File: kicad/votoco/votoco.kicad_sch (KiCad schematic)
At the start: 98 parts, among them J1 Conn_01x02, J10 Conn_01x02, J11 Conn_01x02, J12 Conn_01x02, J13 Conn_01x02, J14 Conn_01x02, J2 Conn_01x04, J3 Conn_02x05_Odd_Even, J4 Conn_01x03, J5 Conn_01x02, J6 Conn_01x02, J7 Conn_01x02, J8 Conn_01x03, J9 USB_B_Micro, Q1 RQ6E045TN, Q2 RQ6E045TN, Q3 RQ6E045TN, SW1 Reset, SW2 Boot, U1 SN65HVD231, U2 TMC2209-LA-T, U3 STM32F042G6Ux, U4 74AHC1G08, U5 MAX2040xAFL, U6 NCP1117-3.3, U7 ADXL345BCCZ, Y1 12Mhz

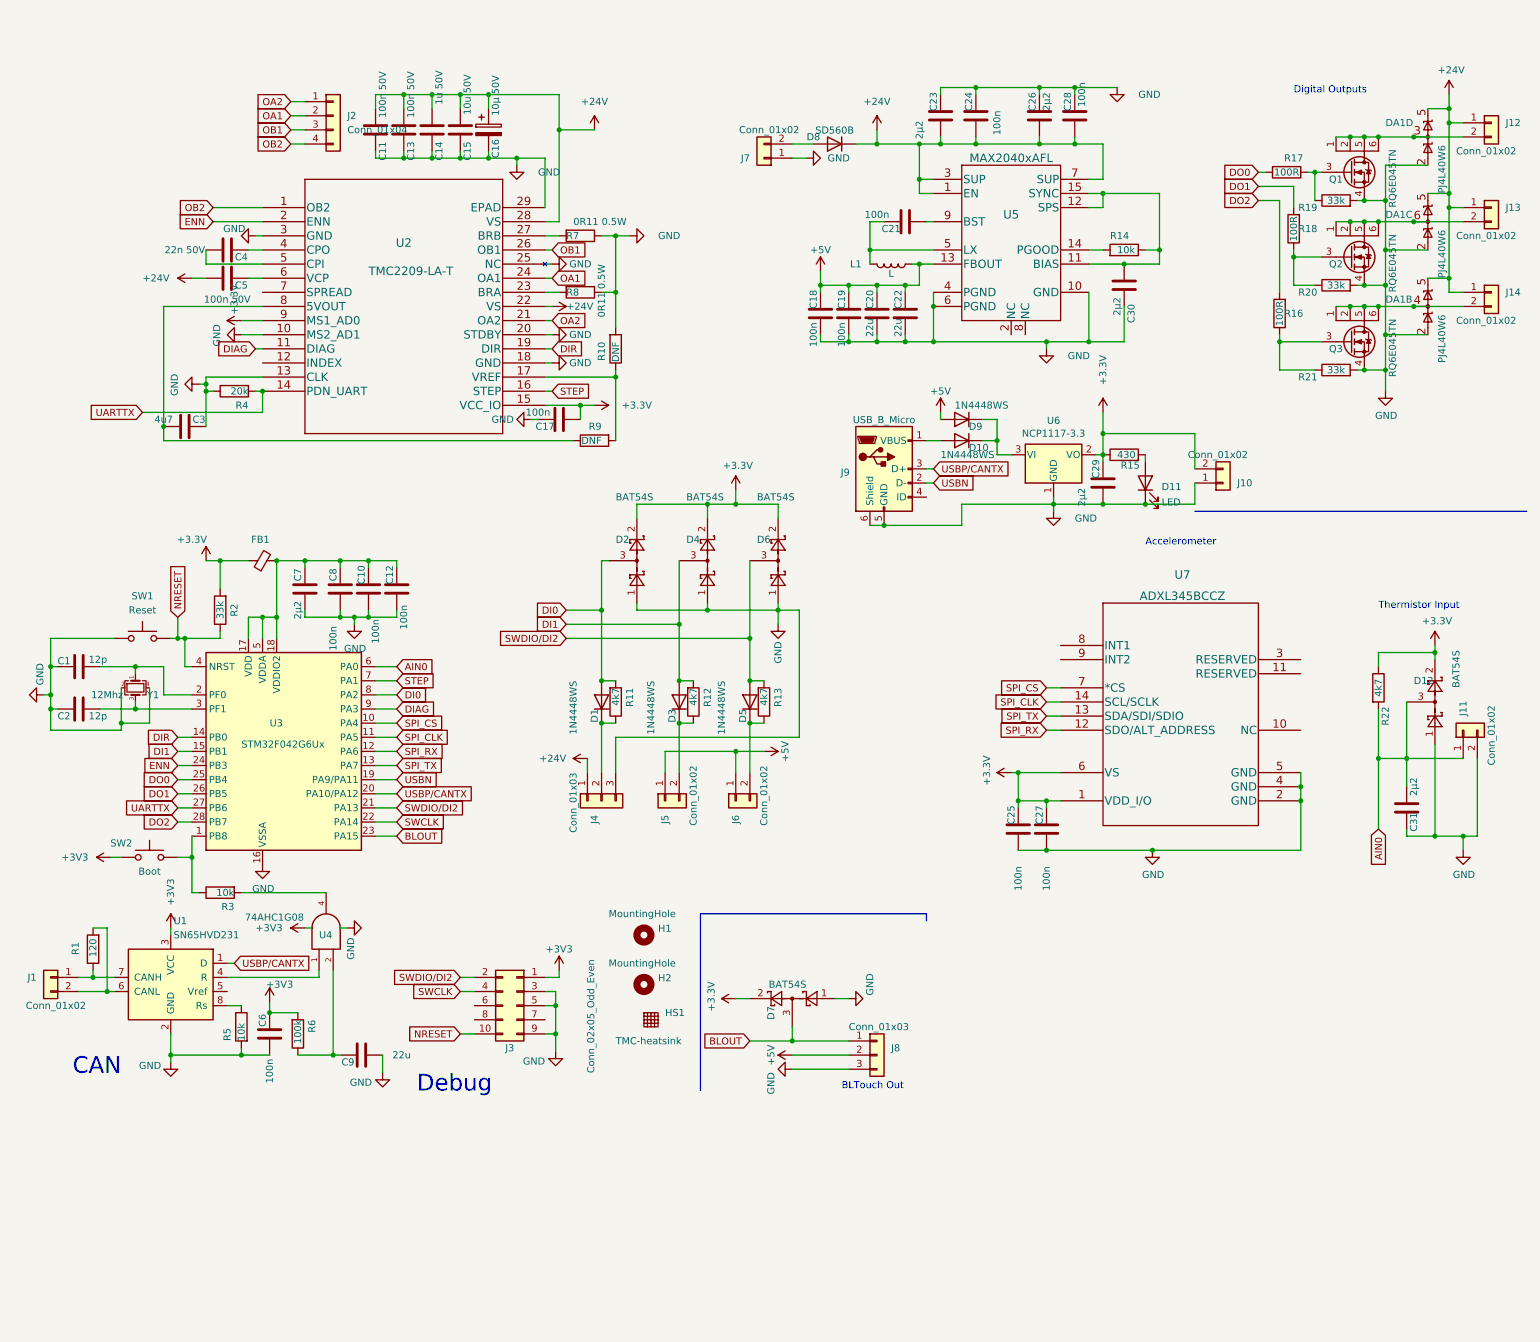
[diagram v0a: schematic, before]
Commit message: some error from V1.0 corrected
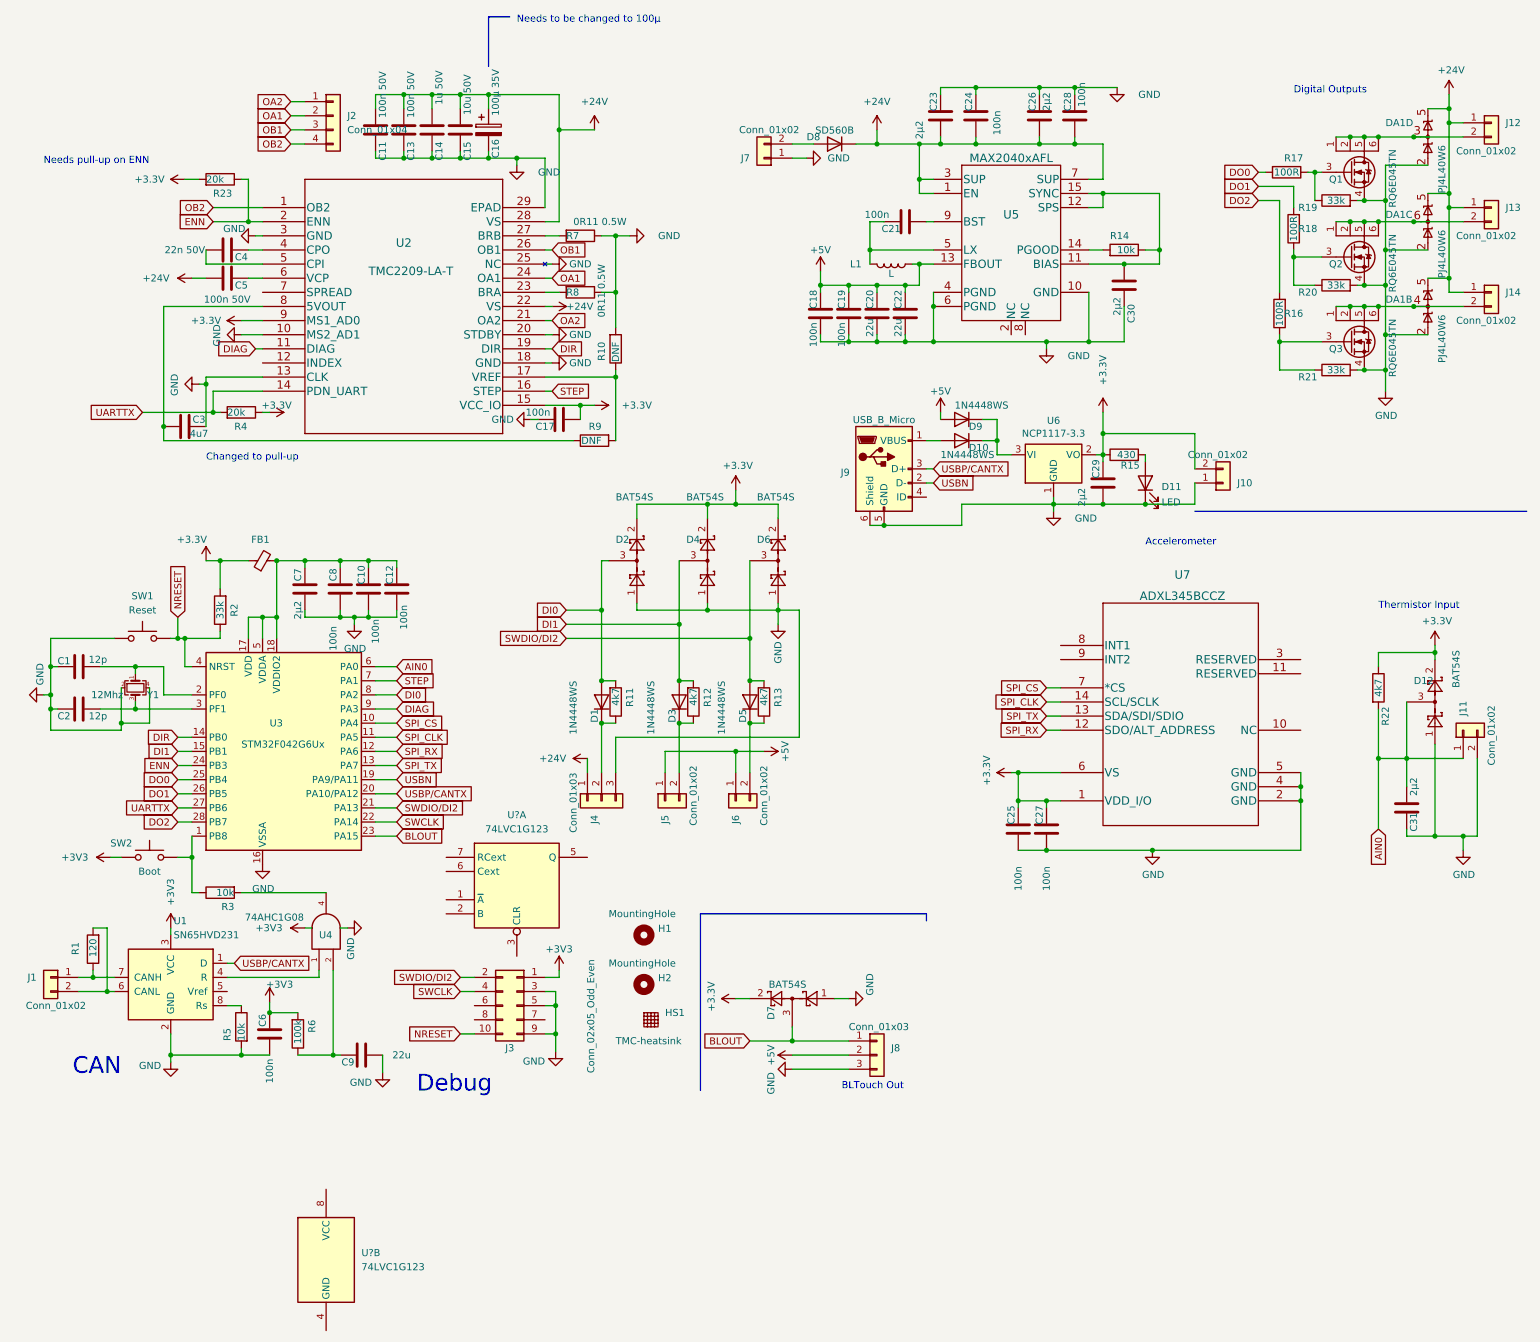
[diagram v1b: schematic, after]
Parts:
- added R23: 20k, Resistor_SMD:R_0603_1608Metric, symbol Device:R
- added U? (x2): 74LVC1G123, symbol 74xGxx:74LVC1G123
- C16: value 10µ 50V -> 100µ 35V; footprint Capacitor_SMD:CP_Elec_4x3 -> Capacitor_SMD:CP_Elec_6.3x7.7
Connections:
- net +3V3: now also R4.1, R23.2
- net ENN: now also R23.1
- net GND: no longer R4.1
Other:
- note added: "Changed to pull-up"
- note added: "Needs pull-up on ENN"
- note added: "Needs to be changed to 100µ"
- moved on the sheet: R4

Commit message: switched to new mcu
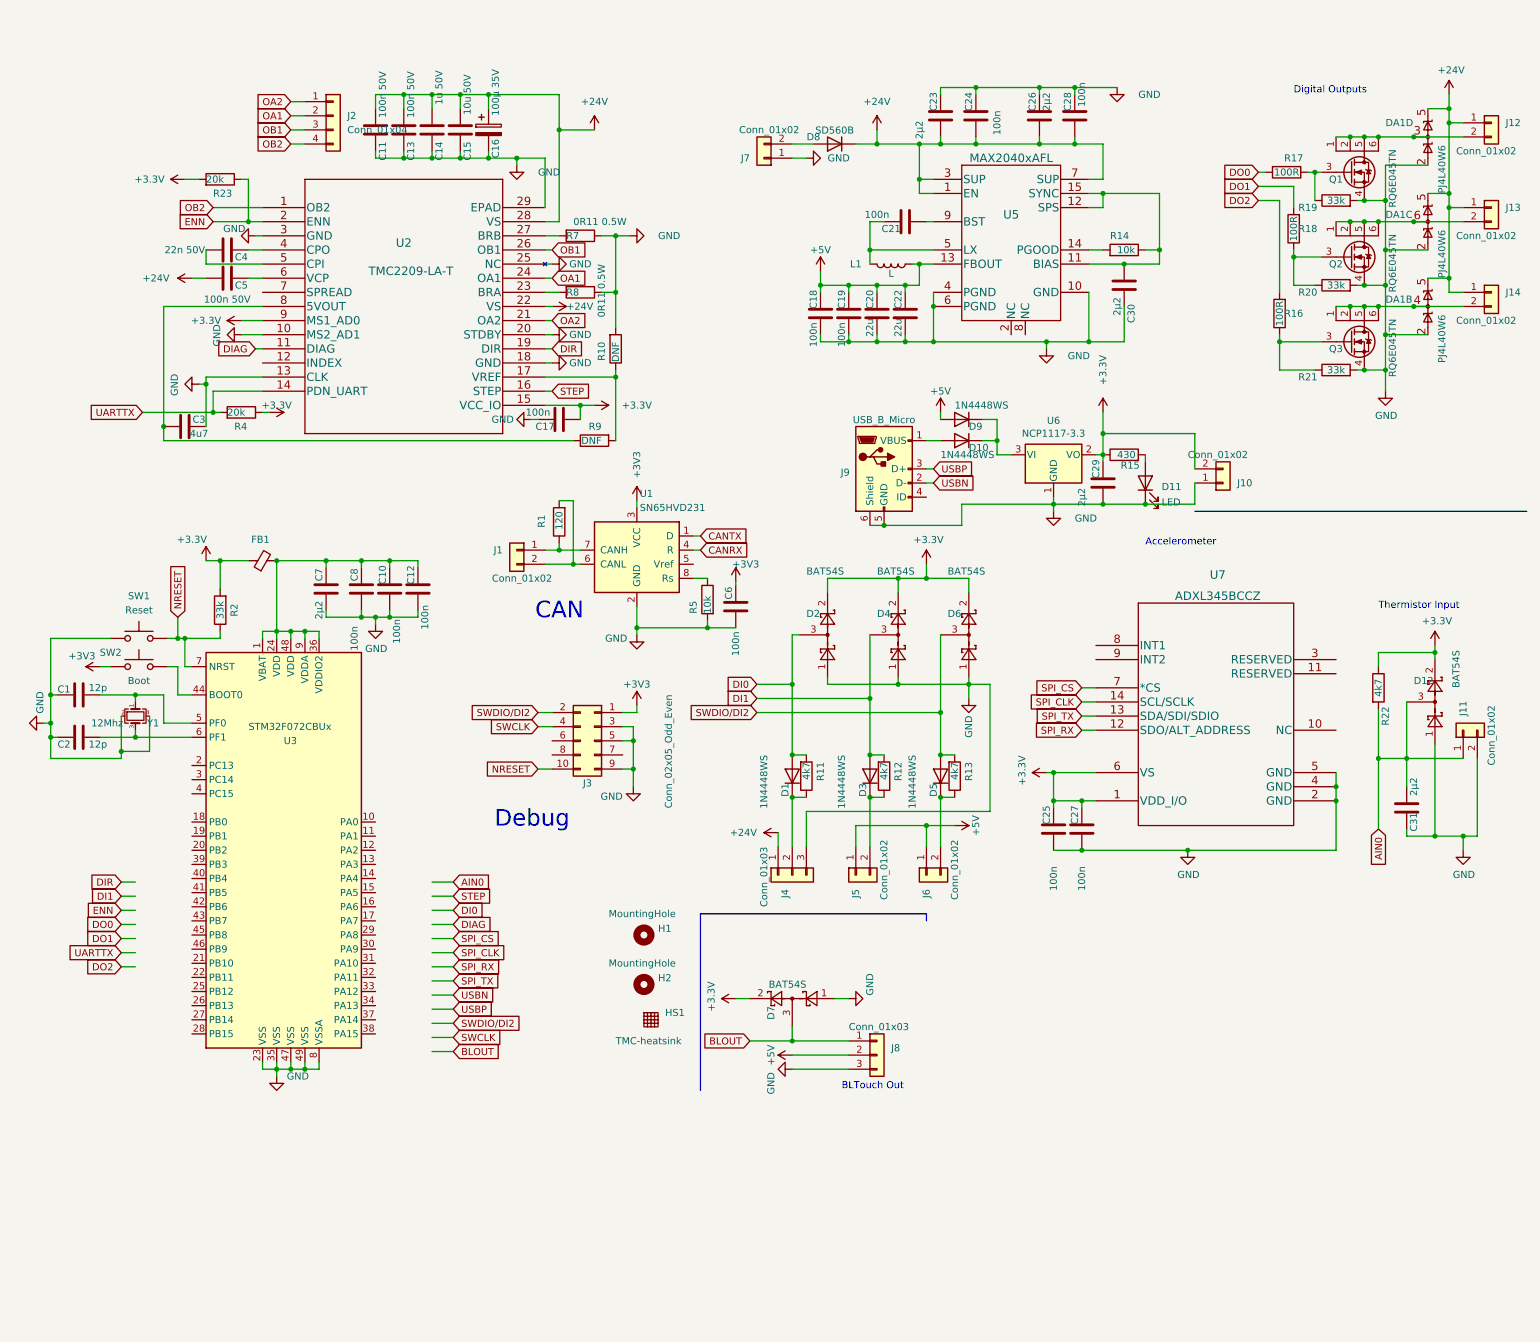
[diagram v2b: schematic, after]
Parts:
- removed C9: 22u, Capacitor_SMD:C_0603_1608Metric, symbol Device:C
- removed R3: 10k, Resistor_SMD:R_0603_1608Metric, symbol Device:R
- removed R6: 100k, Resistor_SMD:R_0603_1608Metric, symbol Device:R
- removed U3: STM32F042G6Ux, Package_DFN_QFN:QFN-28_4x4mm_P0.5mm, symbol MCU_ST_STM32F0:STM32F042G6Ux
- removed U4: 74AHC1G08, Package_TO_SOT_SMD:SOT-353_SC-70-5, symbol 74xGxx:74AHC1G08
- removed U? (x2): 74LVC1G123, symbol 74xGxx:74LVC1G123
- added U3: STM32F072CBUx, Package_DFN_QFN:QFN-48-1EP_7x7mm_P0.5mm_EP5.6x5.6mm, symbol MCU_ST_STM32F0:STM32F072CBUx
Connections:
- net GND: now also U3.23 (VSS), U3.35 (VSS), U3.47 (VSS), U3.49 (VSS), U3.8 (VSSA)
- net NRESET: now also U3.7 (NRST)
- net at C10.1, C12.1, C7.1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: now also U3.1 (VBAT), U3.24 (VDD), U3.36 (VDDIO2), U3.48 (VDD), U3.9 (VDDA)
- net at SW2.2: now also U3.44 (BOOT0)
- net at C1.2, Y1.1: now also U3.5 (PF0)
- net at C2.2, Y1.3: now also U3.6 (PF1)
- net CANRX: now reaches U1.4 (R)
- net USBP/CANTX renamed CANTX
- net CANTX: no longer J9.3 (D+)
- new net USBP: J9.3 (D+)
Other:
- note removed: "Changed to pull-up"
- note removed: "Needs pull-up on ENN"
- note removed: "Needs to be changed to 100µ"
- moved on the sheet: C1, C10, C12, C2, C25, C27, C6, C7, C8, D1, D2, D3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

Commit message: temp sensor added / I2C connector added / layout almost finished
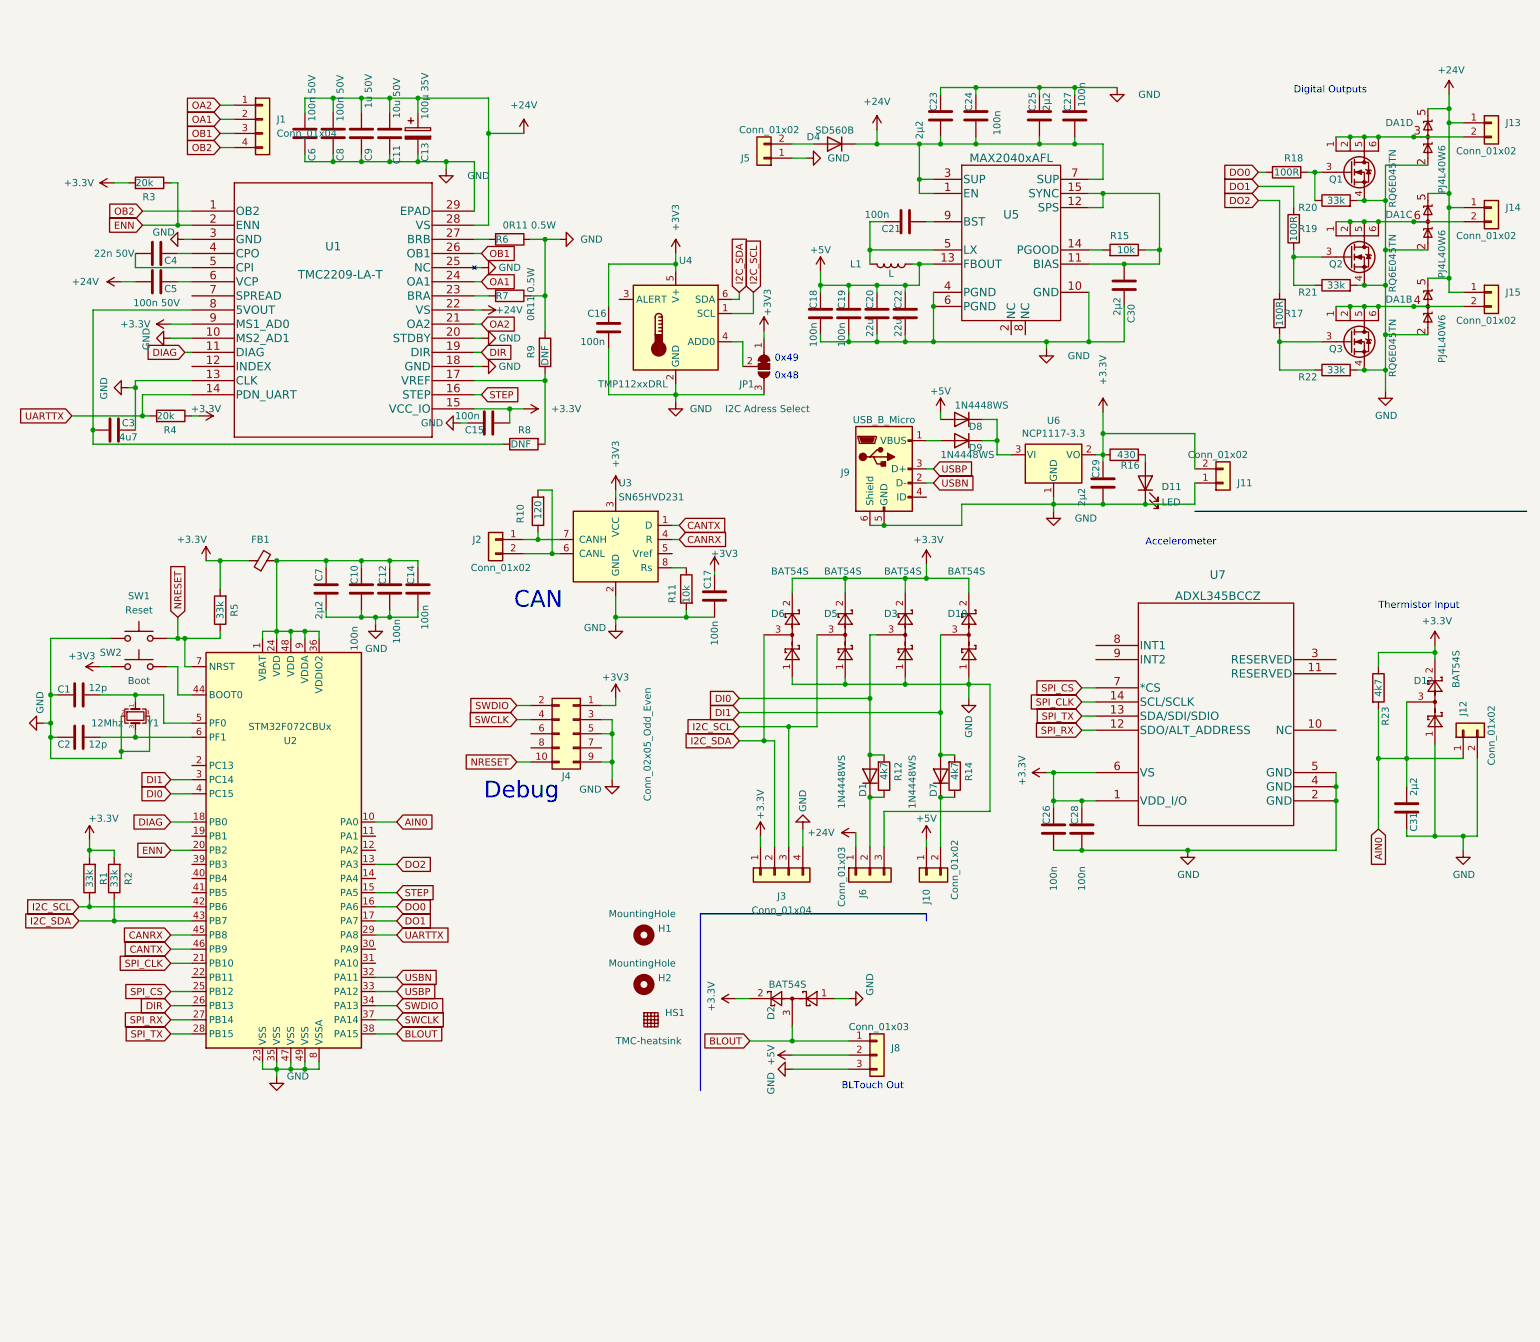
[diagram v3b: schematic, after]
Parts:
- removed D3: 1N4448WS, Diode_SMD:D_SOD-323, symbol Diode:1N4448WS
- removed D4: BAT54S, Package_TO_SOT_SMD:SOT-23, symbol Diode:BAT54S
- removed J5: Conn_01x02, votoco:JST_PH_B2B-PH-SM4-TB_1x02-1MP_P2.00mm_Vertical, symbol Connector_Generic:Conn_01x02
- removed R12: 4k7, Resistor_SMD:R_0603_1608Metric, symbol Device:R
- added C16: 100n, Capacitor_SMD:C_0603_1608Metric_Pad1.08x0.95mm_HandSolder, symbol Device:C
- added D5, D6: BAT54S, Package_TO_SOT_SMD:SOT-23, symbol Diode:BAT54S
- added J3: Conn_01x04, votoco:JST_PH_B4B-PH-SM4-TB_1x04-1MP_P2.00mm_Vertical, symbol Connector_Generic:Conn_01x04
- added JP1: I2C Adress Select, Jumper:SolderJumper-3_P1.3mm_Bridged12_RoundedPad1.0x1.5mm, symbol Jumper:SolderJumper_3_Bridged12
- added R1, R2: 33k, Resistor_SMD:R_0603_1608Metric, symbol Device:R
- added U4: TMP112xxDRL, Package_TO_SOT_SMD:SOT-563, symbol Sensor_Temperature:TMP112xxDRL
- U2: renamed from U3; footprint Package_DFN_QFN:QFN-48-1EP_7x7mm_P0.5mm_EP5.6x5.6mm -> Library:UFQFPN-48_EP_7x7_Pitch0.5mm
- renumbered C8 to C10, C15 to C11, C10 to C12, C16 to C13, C12 to C14, C17 to C15, C6 to C17, C26 to C25, C25 to C26, C28 to C27, C27 to C28, C11 to C6, C13 to C8, C14 to C9, D6 to D10, D7 to D2, D2 to D3, D8 to D4, D5 to D7, D9 to D8, D10 to D9, J2 to J1, J6 to J10, J10 to J11, J11 to J12, J12 to J13, J13 to J14, J14 to J15, J1 to J2, J3 to J4, J7 to J5, J4 to J6, R1 to R10, R5 to R11, R11 to R12, R13 to R14, R14 to R15, R15 to R16, R16 to R17, R17 to R18, R18 to R19, R19 to R20, R20 to R21, R21 to R22, R22 to R23, R23 to R3, R2 to R5, R7 to R6, R8 to R7, R9 to R8, R10 to R9, U2 to U1, U1 to U3
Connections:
- net +3V3: now also C16.1, D5.2, D6.2, J3.1 (Pin_1), JP1.1 (A), R1.2, R2.2, U4.5 (V+)
- net AIN0: now also U2.10 (PA0)
- net BLOUT: now also U2.38 (PA15)
- net CANRX: now also U2.45 (PB8)
- net CANTX: now also U2.46 (PB9)
- net DI0: now also U2.4 (PC15)
- net DI1: now also D10.3, D7.2 (A), R14.2, U2.3 (PC14)
- net DIAG: now also U2.18 (PB0)
- net DIR: now also U2.26 (PB13)
- net DO0: now also U2.16 (PA6)
- net DO1: now also U2.17 (PA7)
- net DO2: now also U2.13 (PA3)
- net ENN: now also U2.20 (PB2)
- net GND: now also C16.2, D5.1, D6.1, J3.4 (Pin_4), JP1.3 (B), U4.2 (GND)
- net SPI_CLK: now also U2.21 (PB10)
- net SPI_CS: now also U2.25 (PB12)
- net SPI_RX: now also U2.27 (PB14)
- net SPI_TX: now also U2.28 (PB15)
- net STEP: now also U2.15 (PA5)
- net SWCLK: now also U2.37 (PA14)
- net UARTTX: now also U2.29 (PA8)
- net USBN: now also U2.32 (PA11)
- net USBP: now also U2.33 (PA12)
- net SWDIO: now reaches U2.34 (PA13)
- net SWDIO: now also J4.2 (Pin_2)
- net I2C_SCL: now reaches U2.42 (PB6)
- net I2C_SCL: now also D5.3, J3.3 (Pin_3), R1.1, U4.1 (SCL)
- net I2C_SDA: now reaches U2.43 (PB7)
- net I2C_SDA: now also D6.3, J3.2 (Pin_2), R2.1, U4.6 (SDA)
- removed net SWDIO/DI2: D10.3, D7.2 (A), J4.2 (Pin_2), R14.2
- new net: JP1.2 (C), U4.4 (ADD0)
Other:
- note added: "0x48"
- note added: "0x49"
- moved on the sheet: C11, C13, C15, C17, C3, C4, C5, C6, C8, C9, D1, D3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

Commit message: boot0 pull-down-added / uart-tx corrected
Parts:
- added R13: 33k, Resistor_SMD:R_0603_1608Metric, symbol Device:R
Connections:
- net GND: now also R13.2
- net UARTTX: now also U2.30 (PA9); no longer U2.29 (PA8)
- net at SW2.2, U2.44 (BOOT0): now also R13.1
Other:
- moved on the sheet: C10, C12, C14, C7, FB1, R5, SW1, SW2
